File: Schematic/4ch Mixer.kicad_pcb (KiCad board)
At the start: 2 copper layers, 30 x 100 mm, 44 parts, among them P1 Power, U1 TL074, U2 TL072

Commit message: Add input clamp protection and Schentronics logo footprints
Schematic: 1N4148 clamps and 1k series resistors on the inputs.
Library: all four Schentronics logo variants from NTSFootprints.
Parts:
- added D10: 1N4148, Diode_SMD:D_SOD-323, B.Cu at (120.8, 97.3)
- added D3: 1N4148, Diode_SMD:D_SOD-323, B.Cu at (128.0, 93.2)
- added D4: 1N4148, Diode_SMD:D_SOD-323, B.Cu at (125.6, 93.2)
- added D5: 1N4148, Diode_SMD:D_SOD-323, B.Cu at (123.2, 93.2)
- added D6: 1N4148, Diode_SMD:D_SOD-323, B.Cu at (120.8, 93.2)
- added D7: 1N4148, Diode_SMD:D_SOD-323, B.Cu at (128.0, 97.3)
- added D8: 1N4148, Diode_SMD:D_SOD-323, B.Cu at (125.6, 97.3)
- added D9: 1N4148, Diode_SMD:D_SOD-323, B.Cu at (123.2, 97.3)
- added G***: LOGO, _NTSFootprints:SchentronicsLogoSmed, B.Cu at (111.4, 54.4)
- added R20: 1k, Resistor_SMD:R_0805_2012Metric, B.Cu at (123.0, 59.5)
- added R21: 1k, Resistor_SMD:R_0805_2012Metric, B.Cu at (123.0, 83.9)
- added R22: 1k, Resistor_SMD:R_0805_2012Metric, B.Cu at (123.0, 107.4)
- added R23: 1k, Resistor_SMD:R_0805_2012Metric, B.Cu at (107.2, 116.7)
- R18, R19: value 100 -> 1k
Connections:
- RV1 pad 2: Net-(U1A-+) -> Net-(R20-~-Pad2)
- RV2 pad 2: Net-(U1B-+) -> Net-(R21-~-Pad2)
- RV3 pad 2: Net-(U1C-+) -> Net-(R22-~-Pad2)
- RV4 pad 2: Net-(U1D-+) -> Net-(R23-~-Pad2)
- U1 pad 10: Net-(U1C-+) -> Net-(D7-A)
- U1 pad 12: Net-(U1D-+) -> Net-(D10-K)
- U1 pad 3: Net-(U1A-+) -> Net-(D3-A)
- U1 pad 5: Net-(U1B-+) -> Net-(D5-A)
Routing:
- net Net-(U1D-+): track 80.0 -> 0.00 mm, vias 3 -> 0
- net Net-(D10-K): track 0.00 -> 61.8 mm, vias 0 -> 4
- net Net-(D3-A): track 0.00 -> 58.2 mm, vias 0 -> 2
- net Net-(U1C-+): track 51.7 -> 0.00 mm, vias 3 -> 0
- net Net-(D7-A): track 0.00 -> 48.3 mm, vias 0 -> 2
- net Net-(D5-A): track 0.00 -> 40.0 mm, vias 0 -> 2
- net Net-(U1B-+): track 33.6 -> 0.00 mm, vias 1 -> 0
- net +12VA: track 106.4 -> 138.8 mm, vias 2 -> 3
- net -12VA: track 96.2 -> 123.4 mm
- net Net-(R23-~-Pad2): track 0.00 -> 26.1 mm, vias 0 -> 1
- net Net-(U1A-+): track 14.4 -> 0.00 mm, vias 1 -> 0
- net Net-(R22-~-Pad2): track 0.00 -> 3.71 mm
- net Net-(R20-~-Pad2): track 0.00 -> 3.62 mm
- net Net-(R21-~-Pad2): track 0.00 -> 3.22 mm
- net Net-(J3-PadT): track 25.6 -> 26.2 mm, vias 0 -> 1
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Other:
- board text added: "+12V"
- board text added: "-12V"
- board text added: "Red Stripe"

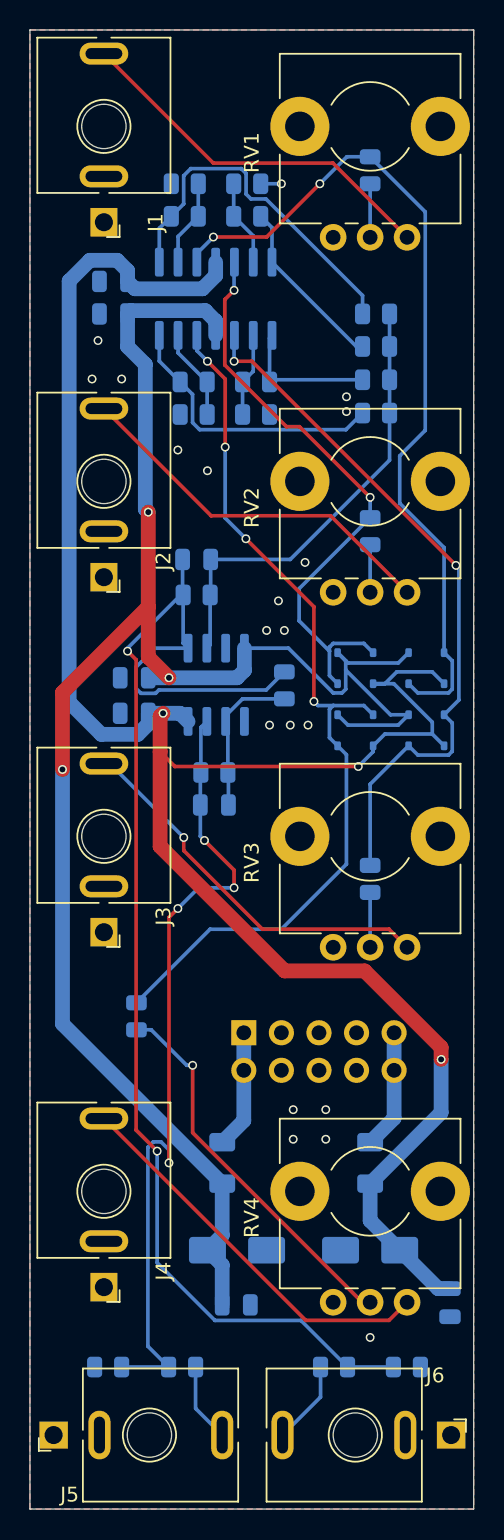
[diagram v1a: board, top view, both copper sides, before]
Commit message: Align passives, add back-side fiducials, and fix routing
Snapped resistor and capacitor columns and rows to shared positions, added
three 1 mm fiducials on the back, and rerouted the affected nets.
DRC: no unconnected items; only starved-thermal warnings remain.
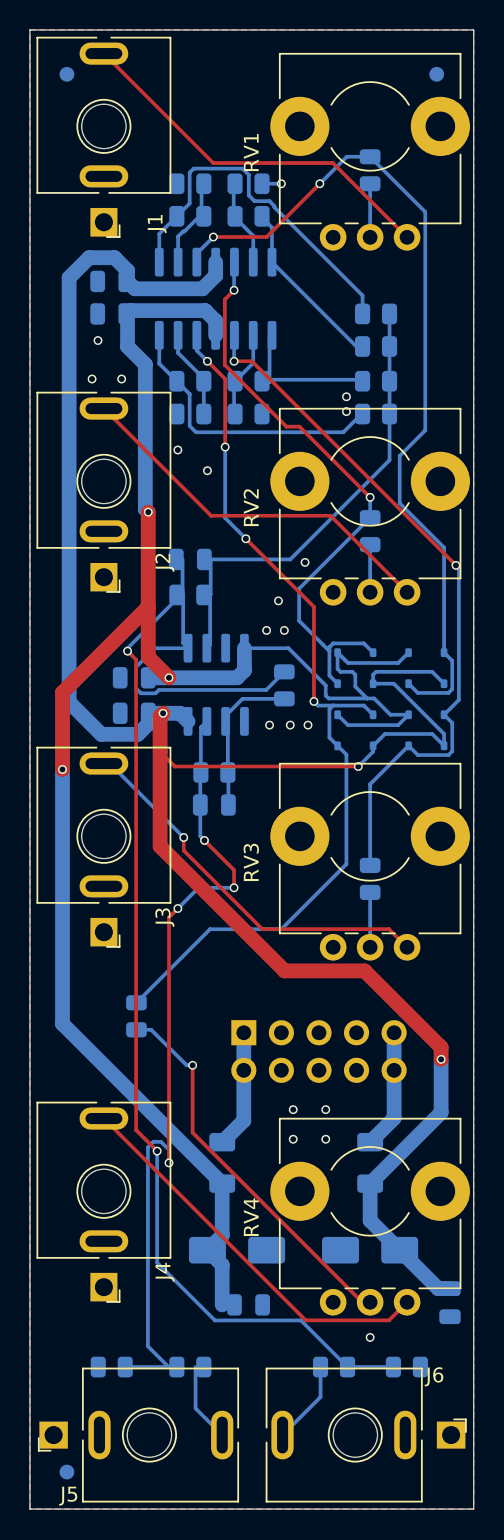
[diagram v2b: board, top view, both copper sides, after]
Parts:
- added FID1: , Fiducial_1mm_Mask2mm, B.Cu at (102.5, 53.0)
- added FID2: , Fiducial_1mm_Mask2mm, B.Cu at (127.5, 53.0)
- added FID3: , Fiducial_1mm_Mask2mm, B.Cu at (102.5, 147.5)
- moved C6 0.83 mm to (114.8, 136.2)
- moved R18 0.56 mm to (110.8, 140.4)
- moved R7 0.51 mm to (114.8, 73.8)
- moved R3 0.51 mm to (114.8, 76.0)
- moved C7 0.43 mm to (110.8, 85.8)
- moved R13 0.43 mm to (110.8, 88.2)
- moved R1 0.37 mm to (110.8, 60.4)
- moved R5 0.37 mm to (110.8, 62.6)
- moved R16 0.24 mm to (105.5, 140.4)
- moved R8 0.23 mm to (110.8, 73.8)
- moved R4 0.23 mm to (110.8, 76.0)
- moved C3 0.12 mm to (105.5, 67.0)
- moved C4 0.12 mm to (105.5, 69.2)
- moved R11 0.10 mm to (123.4, 73.8)
- moved R2 0.09 mm to (114.8, 60.4)
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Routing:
- net -12VA: track 123.4 -> 125.5 mm
- net +12VA: track 138.8 -> 140.6 mm
